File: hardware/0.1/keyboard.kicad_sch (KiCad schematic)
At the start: 327 parts, among them J1 USB_C_Receptacle_USB2.0, J2 SWD, Q1 BSS138, Q2 DTC123J, SW1 RotaryEncoder_Switch, SW10 KEYSW, SW100 KEYSW, SW101 KEYSW, SW102 KEYSW, SW103 KEYSW, SW104 KEYSW, SW105 KEYSW, SW106 KEYSW, SW107 KEYSW, SW108 KEYSW, SW109 KEYSW, SW11 KEYSW, SW110 KEYSW, SW111 KEYSW, SW112 KEYSW, SW113 KEYSW, SW114 KEYSW, SW115 KEYSW, SW116 KEYSW, SW117 KEYSW, SW118 KEYSW, SW119 KEYSW, SW12 KEYSW, SW120 KEYSW, SW121 KEYSW, SW122 KEYSW, SW123 KEYSW, SW124 RotaryEncoder_Switch, SW125 KEYSW, SW126 KEYSW, SW127 KEYSW, SW128 KEYSW, SW129 KEYSW, SW13 KEYSW, SW14 KEYSW, SW15 KEYSW, SW16 KEYSW, SW17 KEYSW, SW18 KEYSW, SW19 KEYSW, SW2 KEYSW, SW20 KEYSW, SW21 KEYSW, SW22 KEYSW, SW23 KEYSW, SW24 KEYSW, SW25 KEYSW, SW26 KEYSW, SW27 KEYSW, SW28 KEYSW, SW29 KEYSW, SW3 KEYSW, SW30 KEYSW, SW31 KEYSW, SW32 KEYSW, SW33 KEYSW, SW34 KEYSW, SW35 KEYSW, SW36 KEYSW, SW37 KEYSW, SW38 KEYSW, SW39 KEYSW, SW4 KEYSW, SW40 KEYSW, SW41 KEYSW, SW42 KEYSW, SW43 KEYSW, SW44 KEYSW, SW45 KEYSW, SW46 KEYSW, SW47 KEYSW, SW48 KEYSW, SW49 KEYSW, SW5 KEYSW, SW50 KEYSW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

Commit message: WIP layout
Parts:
- removed H1, H10, H11, H12, H2, H3, H4, H5, H6, H7, H8, H9: 3.5mm ID, MountingHole:MountingHole_3.5mm, symbol Mechanical:MountingHole
- removed J2: SWD, josh-connectors:4_PIN_THT_Staggered, symbol Connector:Conn_01x04_Male
- added J2: SWD, josh-connectors:5_PIN_THT_Staggered, symbol Connector:Conn_01x05_Male
- SW111: footprint josh-keyboard:MXOnly-1.75U-NoLED -> josh-keyboard:MXOnly-1U-NoLED
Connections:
- net USB_D+ is gone; now on net USB+: R7.2, U3.45 (PA12)
- net USB_D- is gone; now on net USB-: U3.44 (PA11)
- net +3V3: now also J2.5 (Pin_5)
- net BUZZER: now also U3.20 (PA4)
- net ENC0_A: no longer U3.34 (PB13)
- net ENC0_B: no longer U3.35 (PB14)
- net ENC1_A: no longer U3.38 (PC7)
- net ENC1_B: no longer U3.39 (PC8)
- net GND: now also J2.3 (Pin_3)
- net SWDCLK: now also J2.4 (Pin_4)
- net SWDIO: now also J2.2 (Pin_2)
- net col0: no longer U3.33 (PB12)
- net col1: no longer U3.30 (PB11)
- net col10: now also SW56.1 (COL), SW63.1 (COL); no longer SW70.1 (COL), SW71.1 (COL), SW77.1 (COL), U3.2 (PC13)
- net col11: now also SW69.1 (COL); no longer U3.3 (PC14)
- net col12: no longer SW83.1 (COL), SW84.1 (COL), SW90.1 (COL), U3.4 (PC15)
- net col13: now also SW70.1 (COL), SW71.1 (COL), SW77.1 (COL); no longer D102.1 (K), D107.1 (K), D112.1 (K), D118.1 (K), D124.1 (K), D128.1 (K), D15.1 (K), D25.1 (K), D33.1 (K), D4.1 (K), D42.1 (K), D49.1 (K), D58.1 (K), D65.1 (K), D71.1 (K), D78.1 (K), D84.1 (K), D90.1 (K), D95.1 (K), SW128.1 (COL), SW43.1 (COL), SW44.1 (COL), SW45.1 (COL), SW46.1 (COL), SW47.1 (COL), SW48.1 (COL), U3.11 (PC3), U3.17 (PA3), U3.26 (PB0)
- net col14: now also SW83.1 (COL), SW84.1 (COL), SW90.1 (COL); no longer U3.22 (PA6)
- net col15: no longer U3.23 (PA7)
- net col16: no longer U3.24 (PC4)
- net col17: no longer SW113.1 (COL), SW116.1 (COL), SW118.1 (COL), U3.55 (PB3)
- net col18: now also SW113.1 (COL), SW116.1 (COL), SW118.1 (COL); no longer SW123.1 (COL), U3.56 (PB4)
- net col19: now also SW123.1 (COL); no longer U3.57 (PB5)
- net col2: no longer U3.29 (PB10)
- net col3: no longer U3.28 (PB2)
- net col4: no longer U3.62 (PB9)
- net col5: no longer U3.61 (PB8)
- net col7: no longer U3.10 (PC2)
- net col8: no longer SW56.1 (COL), SW63.1 (COL), U3.9 (PC1)
- net col9: no longer SW69.1 (COL), U3.8 (PC0)
- net nRST: now also J2.1 (Pin_1)
- net row0: no longer U3.51 (PC10)
- net row1: no longer U3.52 (PC11)
- net row2: no longer U3.53 (PC12)
- net row3: no longer U3.27 (PB1)
- net row5: no longer U3.25 (PC5)
- net underglow renamed RGB_UG
- new net col6: SW128.1 (COL), SW43.1 (COL), SW44.1 (COL), SW45.1 (COL), SW46.1 (COL), SW47.1 (COL), SW48.1 (COL)
- new net row4: D102.1 (K), D107.1 (K), D112.1 (K), D118.1 (K), D124.1 (K), D128.1 (K), D15.1 (K), D25.1 (K), D33.1 (K), D4.1 (K), D42.1 (K), D49.1 (K), D58.1 (K), D65.1 (K), D71.1 (K), D78.1 (K), D84.1 (K), D90.1 (K), D95.1 (K)
- no-connect marks 20 -> 7
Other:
- note removed: "ESC"
- note removed: "Mounting Holes"
- note removed: "Must go on a DAC Pin"
- note removed: "UP"
- moved on the sheet: D120, D123, D125, D128, D129, D72, D79, D85, D96, SW113, SW116, SW118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

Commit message: schematic had unsaved changes
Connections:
- net col15: no longer SW106.1 (COL)
- net col16: now also SW106.1 (COL); no longer SW112.1 (COL)
- net col17: now also SW112.1 (COL)
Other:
- moved on the sheet: D113, D119, SW106, SW112
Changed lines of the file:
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@@
   (junction (at 46.99 83.82) (diameter 0) (color 0 0 0 0)
   )
+  (junction (at 487.68 148.59) (diameter 0) (color 0 0 0 0)
+  )
   (junction (at 340.36 220.98) (diameter 0) (color 0 0 0 0)
   )
@@
   (junction (at 538.48 97.79) (diameter 0) (color 0 0 0 0)
   )
-  (junction (at 462.28 148.59) (diameter 0) (color 0 0 0 0)
-  )
   (junction (at 146.05 83.82) (diameter 0) (color 0 0 0 0)
   )
@@
   (junction (at 222.25 58.42) (diameter 0) (color 0 0 0 0)
   )
-  (junction (at 476.25 185.42) (diameter 0) (color 0 0 0 0)
-  )
   (junction (at 425.45 83.82) (diameter 0) (color 0 0 0 0)
   )
@@
   (junction (at 349.25 134.62) (diameter 0) (color 0 0 0 0)
   )
-  (junction (at 450.85 185.42) (diameter 0) (color 0 0 0 0)
-  )
   (junction (at 46.99 134.62) (diameter 0) (color 0 0 0 0)
   )
@@
   (junction (at 58.42 93.98) (diameter 0) (color 0 0 0 0)
   )
-  (junction (at 487.68 148.59) (diameter 0) (color 0 0 0 0)
-  )
   (junction (at 157.48 92.71) (diameter 0) (color 0 0 0 0)
   )
@@
   (junction (at 259.08 170.18) (diameter 0) (color 0 0 0 0)
   )
+  (junction (at 476.25 185.42) (diameter 0) (color 0 0 0 0)
+  )
   (junction (at 247.65 109.22) (diameter 0) (color 0 0 0 0)
   )
@@
   (junction (at 259.08 97.79) (diameter 0) (color 0 0 0 0)
   )
+  (junction (at 513.08 147.32) (diameter 0) (color 0 0 0 0)
+  )
   (junction (at 436.88 97.79) (diameter 0) (color 0 0 0 0)
   )
   (junction (at 314.96 234.95) (diameter 0) (color 0 0 0 0)
   )
+  (junction (at 501.65 185.42) (diameter 0) (color 0 0 0 0)
+  )
   (junction (at 411.48 148.59) (diameter 0) (color 0 0 0 0)
   )
@@
     (stroke (width 0) (type default) (color 0 0 0 0))
   )
-  (wire (pts (xy 455.93 173.99) (xy 462.28 173.99))
+  (wire (pts (xy 481.33 173.99) (xy 487.68 173.99))
     (stroke (width 0) (type default) (color 0 0 0 0))
   )
@@
     (stroke (width 0) (type default) (color 0 0 0 0))
   )
+  (wire (pts (xy 501.65 184.15) (xy 501.65 185.42))
+    (stroke (width 0) (type default) (color 0 0 0 0))
+  )
   (wire (pts (xy 158.75 337.82) (xy 158.75 351.79))
     (stroke (width 0) (type default) (color 0 0 0 0))
@@
     (stroke (width 0) (type default) (color 0 0 0 0))
   )
-  (wire (pts (xy 476.25 179.07) (xy 476.25 180.34))
+  (wire (pts (xy 501.65 177.8) (xy 501.65 179.07))
     (stroke (width 0) (type default) (color 0 0 0 0))
   )
@@
     (stroke (width 0) (type default) (color 0 0 0 0))
   )
-  (wire (pts (xy 450.85 179.07) (xy 450.85 180.34))
+  (wire (pts (xy 476.25 179.07) (xy 476.25 180.34))
     (stroke (width 0) (type default) (color 0 0 0 0))
   )
@@
     (stroke (width 0) (type default) (color 0 0 0 0))
   )
-  (wire (pts (xy 425.45 185.42) (xy 450.85 185.42))
+  (wire (pts (xy 425.45 185.42) (xy 476.25 185.42))
     (stroke (width 0) (type default) (color 0 0 0 0))
   )
@@
     (stroke (width 0) (type default) (color 0 0 0 0))
   )
-  (wire (pts (xy 462.28 148.59) (xy 462.28 173.99))
+  (wire (pts (xy 487.68 148.59) (xy 487.68 173.99))
     (stroke (width 0) (type default) (color 0 0 0 0))
   )
@@
     (stroke (width 0) (type default) (color 0 0 0 0))
   )
-  (wire (pts (xy 450.85 185.42) (xy 476.25 185.42))
-    (stroke (width 0) (type default) (color 0 0 0 0))
-  )
   (wire (pts (xy 63.5 219.71) (xy 63.5 224.79))
     (stroke (width 0) (type default) (color 0 0 0 0))
@@
     (stroke (width 0) (type default) (color 0 0 0 0))
   )
-  (wire (pts (xy 481.33 173.99) (xy 487.68 173.99))
+  (wire (pts (xy 506.73 172.72) (xy 513.08 172.72))
     (stroke (width 0) (type default) (color 0 0 0 0))
   )
@@
     (stroke (width 0) (type default) (color 0 0 0 0))
   )
-  (wire (pts (xy 476.25 185.42) (xy 527.05 185.42))
-    (stroke (width 0) (type default) (color 0 0 0 0))
-  )
   (wire (pts (xy 72.39 219.71) (xy 73.66 219.71))
     (stroke (width 0) (type default) (color 0 0 0 0))
@@
     (stroke (width 0) (type default) (color 0 0 0 0))
   )
-  (wire (pts (xy 487.68 148.59) (xy 487.68 173.99))
+  (wire (pts (xy 513.08 147.32) (xy 513.08 172.72))
     (stroke (width 0) (type default) (color 0 0 0 0))
   )
@@
     (stroke (width 0) (type default) (color 0 0 0 0))
   )
+  (wire (pts (xy 476.25 185.42) (xy 501.65 185.42))
+    (stroke (width 0) (type default) (color 0 0 0 0))
+  )
   (wire (pts (xy 312.42 234.95) (xy 312.42 236.22))
     (stroke (width 0) (type default) (color 0 0 0 0))
@@
     (stroke (width 0) (type default) (color 0 0 0 0))
   )
+  (wire (pts (xy 501.65 185.42) (xy 527.05 185.42))
+    (stroke (width 0) (type default) (color 0 0 0 0))
+  )
   (polyline (pts (xy 158.75 38.1) (xy 158.75 187.96))
     (stroke (width 0) (type default) (color 0 0 0 0))
@@
     (pin "2")
   )
-  (symbol (lib_id "Device:D_Small") (at 476.25 182.88 90) (unit 1)
+  (symbol (lib_id "Device:D_Small") (at 501.65 181.61 90) (unit 1)
     (in_bom yes) (on_board yes)
-    (property "Reference" "D119" (id 0) (at 478.79 181.102 90)
+    (property "Reference" "D119" (id 0) (at 504.19 179.832 90)
       (effects (font (size 1.27 1.27)) (justify right))
     )
-    (property "Value" "1N4148" (id 1) (at 478.79 183.388 90)
+    (property "Value" "1N4148" (id 1) (at 504.19 182.118 90)
       (effects (font (size 1.27 1.27)) (justify right))
     )
-    (property "Footprint" "Diode_SMD:D_SOD-123" (id 2) (at 477.52 190.5 0)
+    (property "Footprint" "Diode_SMD:D_SOD-123" (id 2) (at 502.92 189.23 0)
       (effects (font (size 1.27 1.27)) hide)
     )
-    (property "Datasheet" "~" (id 3) (at 477.52 190.5 0)
+    (property "Datasheet" "~" (id 3) (at 502.92 189.23 0)
       (effects (font (size 1.27 1.27)) hide)
     )
@@
     (pin "2")
   )
-  (symbol (lib_id "josh-keyboard:MX-NoLED") (at 477.52 175.26 0) (unit 1)
+  (symbol (lib_id "josh-keyboard:MX-NoLED") (at 502.92 173.99 0) (unit 1)
     (in_bom yes) (on_board yes)
-    (property "Reference" "SW112" (id 0) (at 483.87 172.72 0)
+    (property "Reference" "SW112" (id 0) (at 509.27 171.45 0)
       (effects (font (size 1.524 1.524)))
     )
-    (property "Value" "KEYSW" (id 1) (at 477.52 177.8 0)
+    (property "Value" "KEYSW" (id 1) (at 502.92 176.53 0)
       (effects (font (size 1.524 1.524)) hide)
     )
-    (property "Footprint" "josh-keyboard:MXOnly-1U-NoLED" (id 2) (at 477.52 175.26 0)
+    (property "Footprint" "josh-keyboard:MXOnly-1U-NoLED" (id 2) (at 502.92 173.99 0)
       (effects (font (size 1.524 1.524)) hide)
     )
-    (property "Datasheet" "" (id 3) (at 477.52 175.26 0)
+    (property "Datasheet" "" (id 3) (at 502.92 173.99 0)
       (effects (font (size 1.524 1.524)))
     )
@@
     (pin "2")
   )
-  (symbol (lib_id "Device:D_Small") (at 450.85 182.88 90) (unit 1)
+  (symbol (lib_id "Device:D_Small") (at 476.25 182.88 90) (unit 1)
     (in_bom yes) (on_board yes)
-    (property "Reference" "D113" (id 0) (at 453.39 181.102 90)
+    (property "Reference" "D113" (id 0) (at 478.79 181.102 90)
       (effects (font (size 1.27 1.27)) (justify right))
     )
-    (property "Value" "1N4148" (id 1) (at 453.39 183.388 90)
+    (property "Value" "1N4148" (id 1) (at 478.79 183.388 90)
       (effects (font (size 1.27 1.27)) (justify right))
     )
-    (property "Footprint" "Diode_SMD:D_SOD-123" (id 2) (at 452.12 190.5 0)
+    (property "Footprint" "Diode_SMD:D_SOD-123" (id 2) (at 477.52 190.5 0)
       (effects (font (size 1.27 1.27)) hide)
     )
-    (property "Datasheet" "~" (id 3) (at 452.12 190.5 0)
+    (property "Datasheet" "~" (id 3) (at 477.52 190.5 0)
       (effects (font (size 1.27 1.27)) hide)
     )
@@
     (pin "1")
   )
-  (symbol (lib_id "josh-keyboard:MX-NoLED") (at 452.12 175.26 0) (unit 1)
+  (symbol (lib_id "josh-keyboard:MX-NoLED") (at 477.52 175.26 0) (unit 1)
     (in_bom yes) (on_board yes)
-    (property "Reference" "SW106" (id 0) (at 458.47 172.72 0)
+    (property "Reference" "SW106" (id 0) (at 483.87 172.72 0)
       (effects (font (size 1.524 1.524)))
     )
-    (property "Value" "KEYSW" (id 1) (at 452.12 177.8 0)
+    (property "Value" "KEYSW" (id 1) (at 477.52 177.8 0)
       (effects (font (size 1.524 1.524)) hide)
     )
-    (property "Footprint" "josh-keyboard:MXOnly-1.5U-NoLED" (id 2) (at 452.12 175.26 0)
+    (property "Footprint" "josh-keyboard:MXOnly-1.5U-NoLED" (id 2) (at 477.52 175.26 0)
       (effects (font (size 1.524 1.524)) hide)
     )
-    (property "Datasheet" "" (id 3) (at 452.12 175.26 0)
+    (property "Datasheet" "" (id 3) (at 477.52 175.26 0)
       (effects (font (size 1.524 1.524)))
     )

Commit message: first pass layout
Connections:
- net ENC0_A: now also U3.29 (PB10)
- net ENC0_B: now also U3.30 (PB11)
- net ENC1_A: now also U3.51 (PC10)
- net ENC1_B: now also U3.52 (PC11)
- net col0: now also U3.25 (PC5)
- net col1: now also U3.24 (PC4)
- net col10: now also U3.33 (PB12)
- net col11: now also U3.3 (PC14)
- net col12: now also U3.62 (PB9)
- net col13: now also U3.61 (PB8)
- net col14: now also U3.59 (PB7)
- net col15: now also U3.58 (PB6)
- net col16: now also U3.57 (PB5)
- net col17: now also U3.56 (PB4)
- net col18: now also U3.55 (PB3)
- net col19: now also U3.53 (PC12)
- net col2: now also U3.23 (PA7)
- net col3: now also U3.22 (PA6)
- net col4: now also U3.40 (PC9)
- net col5: now also U3.39 (PC8)
- net col6: now also U3.38 (PC7)
- net col7: now also U3.37 (PC6)
- net col8: now also U3.35 (PB14)
- net col9: now also U3.34 (PB13)
- net row0: now also U3.42 (PA9)
- net row1: now also U3.41 (PA8)
- net row2: now also U3.50 (PA15)
- net row3: now also U3.2 (PC13)
- net row4: now also U3.4 (PC15)
- net row5: now also U3.8 (PC0)
- no-connect marks 7 -> 9
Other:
- moved on the sheet: BZ1

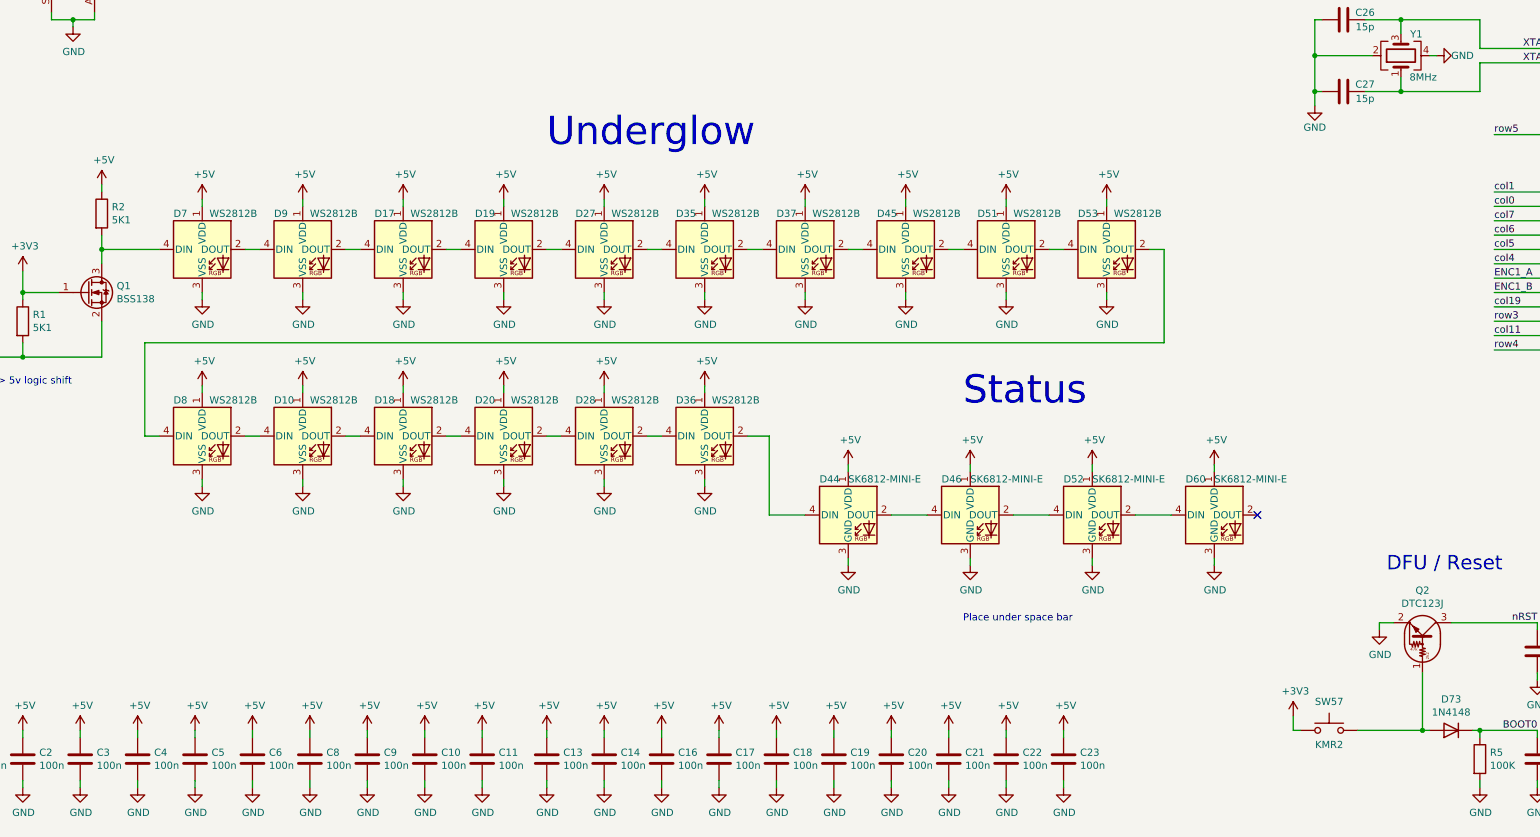
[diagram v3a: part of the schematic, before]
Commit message: added more LEDs
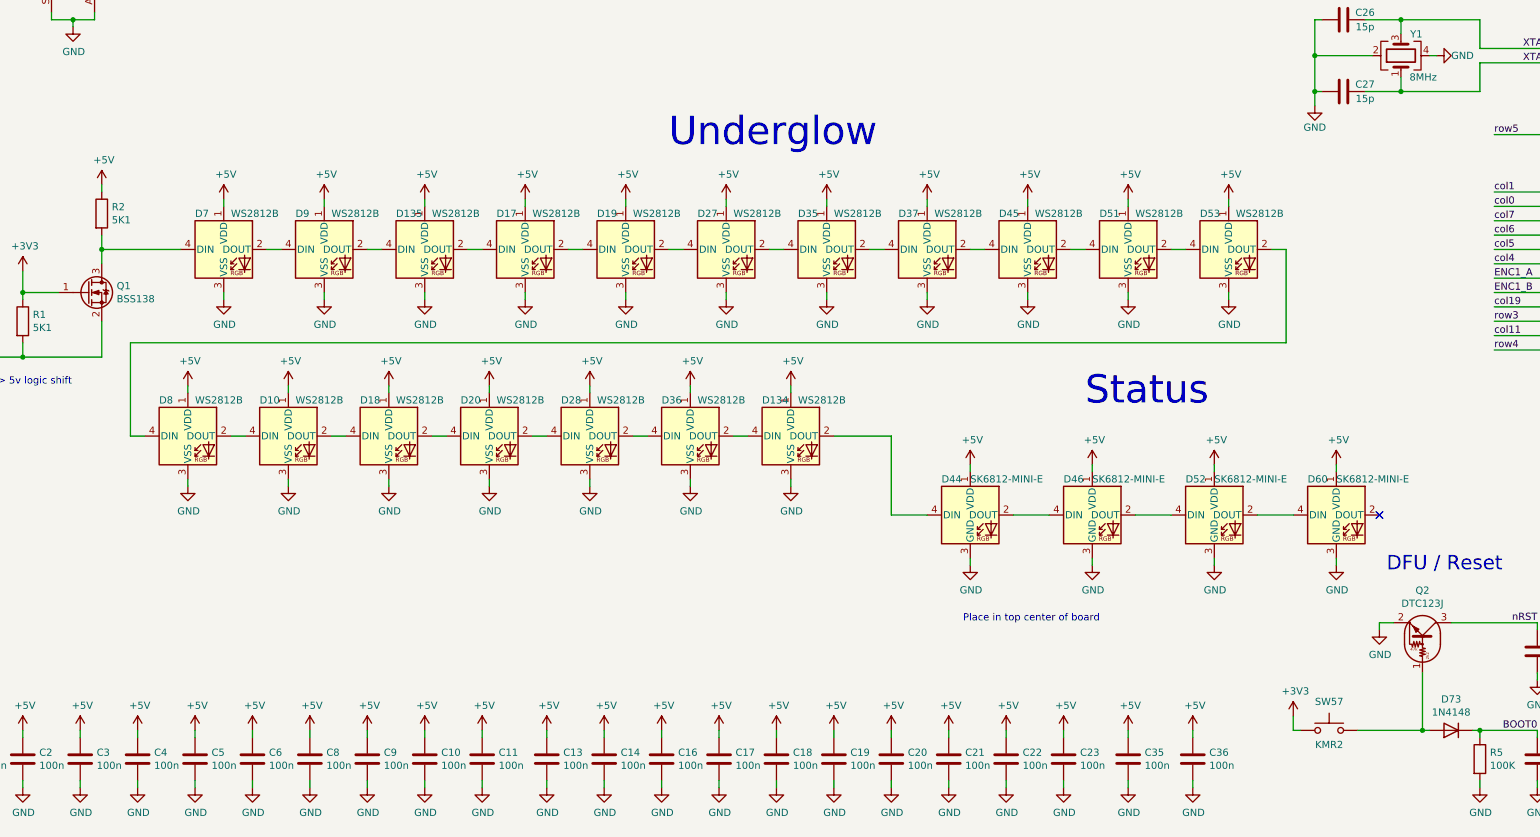
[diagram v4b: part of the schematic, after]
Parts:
- added C35, C36: 100n, Capacitor_SMD:C_0603_1608Metric, symbol Device:C
- added D134, D135: WS2812B, LED_SMD:LED_WS2812B_PLCC4_5.0x5.0mm_P3.2mm, symbol LED:WS2812B
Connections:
- net +5V: now also C35.2, C36.2, D134.1 (VDD), D135.1 (VDD)
- net GND: now also C35.1, C36.1, D134.3 (VSS), D135.3 (VSS)
- net at D9.2 (DOUT): now also D135.4 (DIN); no longer D17.4 (DIN)
- net at D36.2 (DOUT): now also D134.4 (DIN); no longer D44.4 (DIN)
- new net: D135.2 (DOUT), D17.4 (DIN)
- new net: D134.2 (DOUT), D44.4 (DIN)
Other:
- note added: "Place in top center of board"
- note removed: "Place under space bar"
- moved on the sheet: D10, D17, D18, D19, D20, D27, D28, D35, D36, D37, D44, D45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

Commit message: clean up traces, silk TODO
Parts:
- added H1, H2: M2, MountingHole:MountingHole_2.2mm_M2_DIN965_Pad, symbol Mechanical:MountingHole_Pad
- added J3: SPARE, josh-connectors:5_PIN_THT_Staggered, symbol Connector:Conn_01x05_Male
- SW116, SW32: footprint josh-keyboard:MXOnly-2.25U-ReversedStabilizers-NoLED -> josh-keyboard:MXOnly-2.25U-NoLED
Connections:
- net +3V3: now also J3.5 (Pin_5)
- net GND: now also H1.1, H2.1, J3.3 (Pin_3)
- net SPARE_0: now reaches U3.14 (PA0)
- net SPARE_0: now also J3.1 (Pin_1)
- net SPARE_1: now reaches U3.15 (PA1)
- net SPARE_1: now also J3.2 (Pin_2)
- net SPARE_2: now reaches U3.16 (PA2)
- net SPARE_2: now also J3.4 (Pin_4)
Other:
- note added: "Mounting Holes"
- note added: "Spare IO"
- moved on the sheet: BZ1, C24, C25, C26, C27, C28, C29, C30, C31, C32, C33, C34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

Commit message: add silk
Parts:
- LOGO3: footprint josh-logos:OSHW_Logo_3.6x3.6_F.Mask -> josh-logos:OSHW-Logo2_9.8x8mm_Mask
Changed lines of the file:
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@@
     )
     (property "Value" "OSHW Logo" (id 1) (at 436.88 404.495 0))
-    (property "Footprint" "josh-logos:OSHW_Logo_3.6x3.6_F.Mask" (id 2) (at 436.88 398.78 0)
+    (property "Footprint" "josh-logos:OSHW-Logo2_9.8x8mm_Mask" (id 2) (at 436.88 398.78 0)
       (effects (font (size 1.27 1.27)) hide)
     )
@@
     )
     (path "/00000000-0000-0000-0000-0000619339ec"
-      (reference "LOGO3") (unit 1) (value "OSHW Logo") (footprint "josh-logos:OSHW_Logo_3.6x3.6_F.Mask")
+      (reference "LOGO3") (unit 1) (value "OSHW Logo") (footprint "josh-logos:OSHW-Logo2_9.8x8mm_Mask")
     )
     (path "/00000000-0000-0000-0000-0000619339b0"
